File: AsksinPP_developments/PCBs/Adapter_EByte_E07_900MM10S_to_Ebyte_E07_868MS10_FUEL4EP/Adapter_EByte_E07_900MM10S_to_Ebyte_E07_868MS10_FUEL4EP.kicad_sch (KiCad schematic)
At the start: 15 parts

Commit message: PCBs: updates to promote Adapter_EByte_E07_900MM10S_to_Ebyte_E07_868MS10_FUEL4EP in several PCBs
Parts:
- Module1: LCSC (none) -> C5844212; TYPE (none) -> 10x10mm
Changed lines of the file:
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@@
       (effects (font (size 1.27 1.27)) hide)
+    )
+    (property "LCSC" "C5844212" (at 123.19 91.44 0)
+      (effects (font (size 1.524 1.524)) hide)
+    )
+    (property "TYPE" "10x10mm" (at 123.19 91.44 0)
+      (effects (font (size 1.524 1.524)) hide)
     )
     (pin "1D")

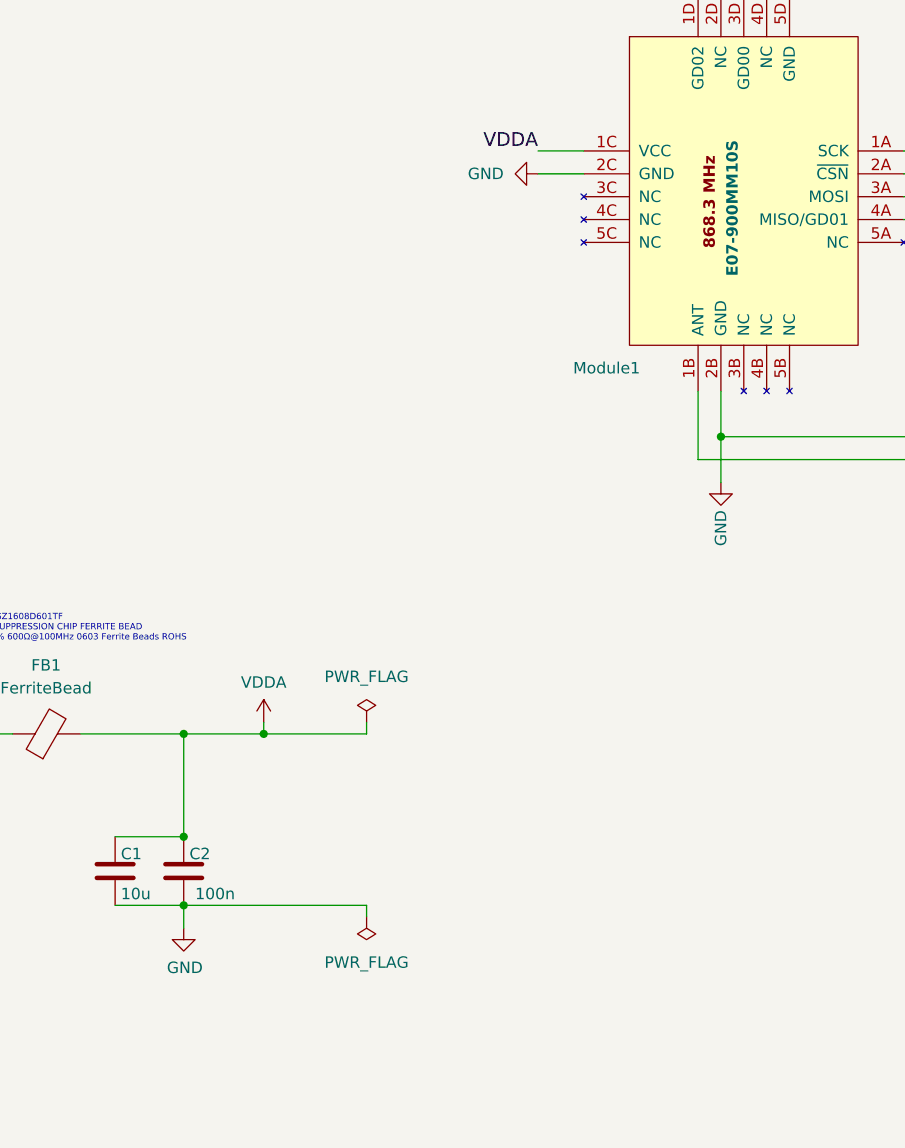
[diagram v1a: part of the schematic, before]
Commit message: PCBs/Adapter_EByte_E07_900MM10S_to_Ebyte_E07_868MS10_FUEL4EP: migration to KiCAD8; order of prototypes at JLCPCB
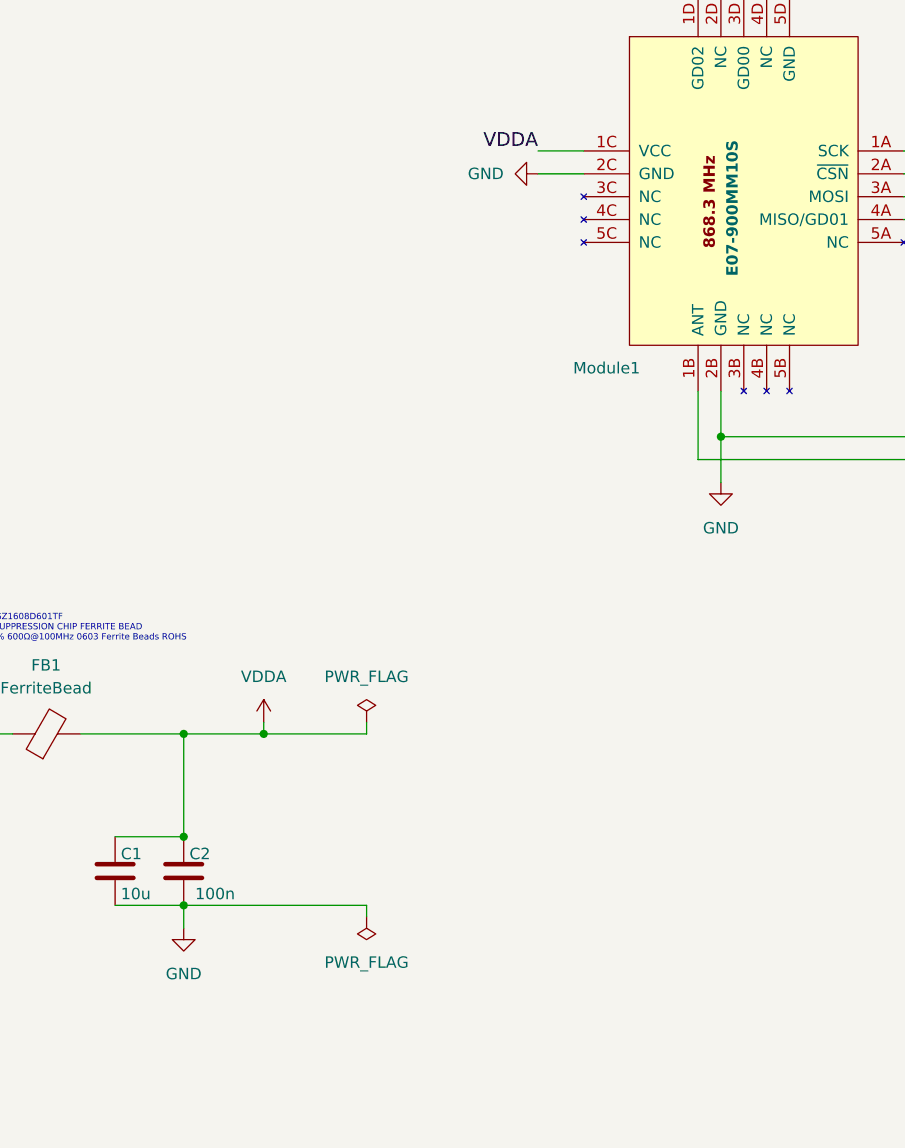
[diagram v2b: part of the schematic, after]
